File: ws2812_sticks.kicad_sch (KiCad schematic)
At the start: 11 parts, among them J1 Conn_01x03_Socket, J2 Conn_01x03_Socket

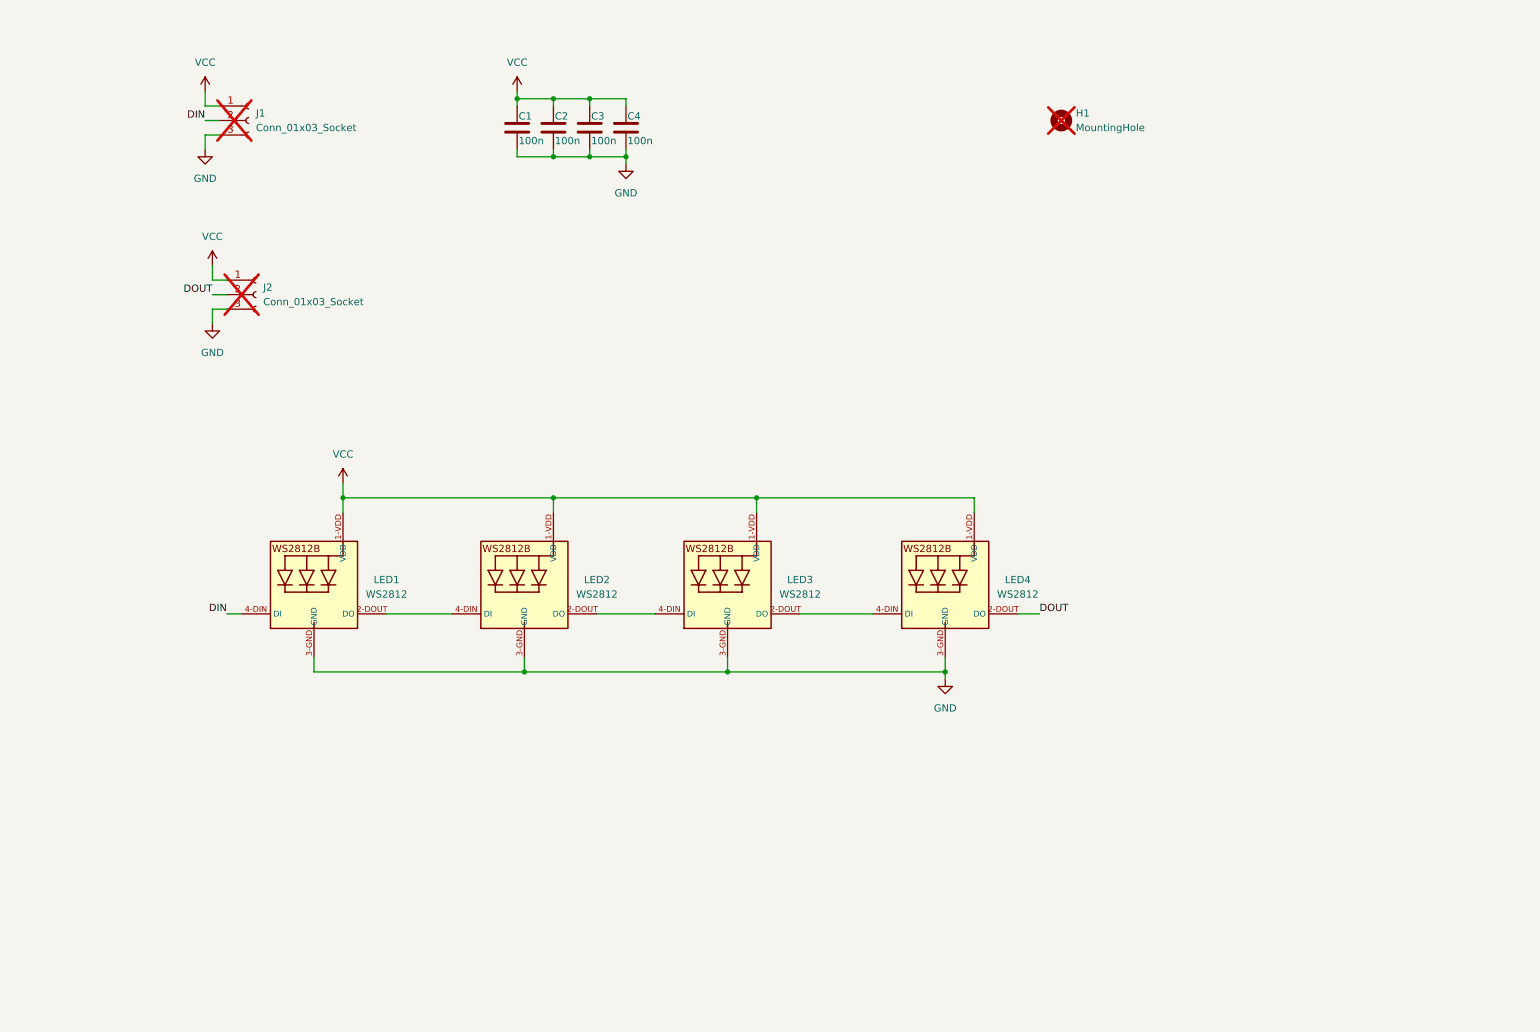
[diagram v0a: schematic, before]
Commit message: created 8 led version
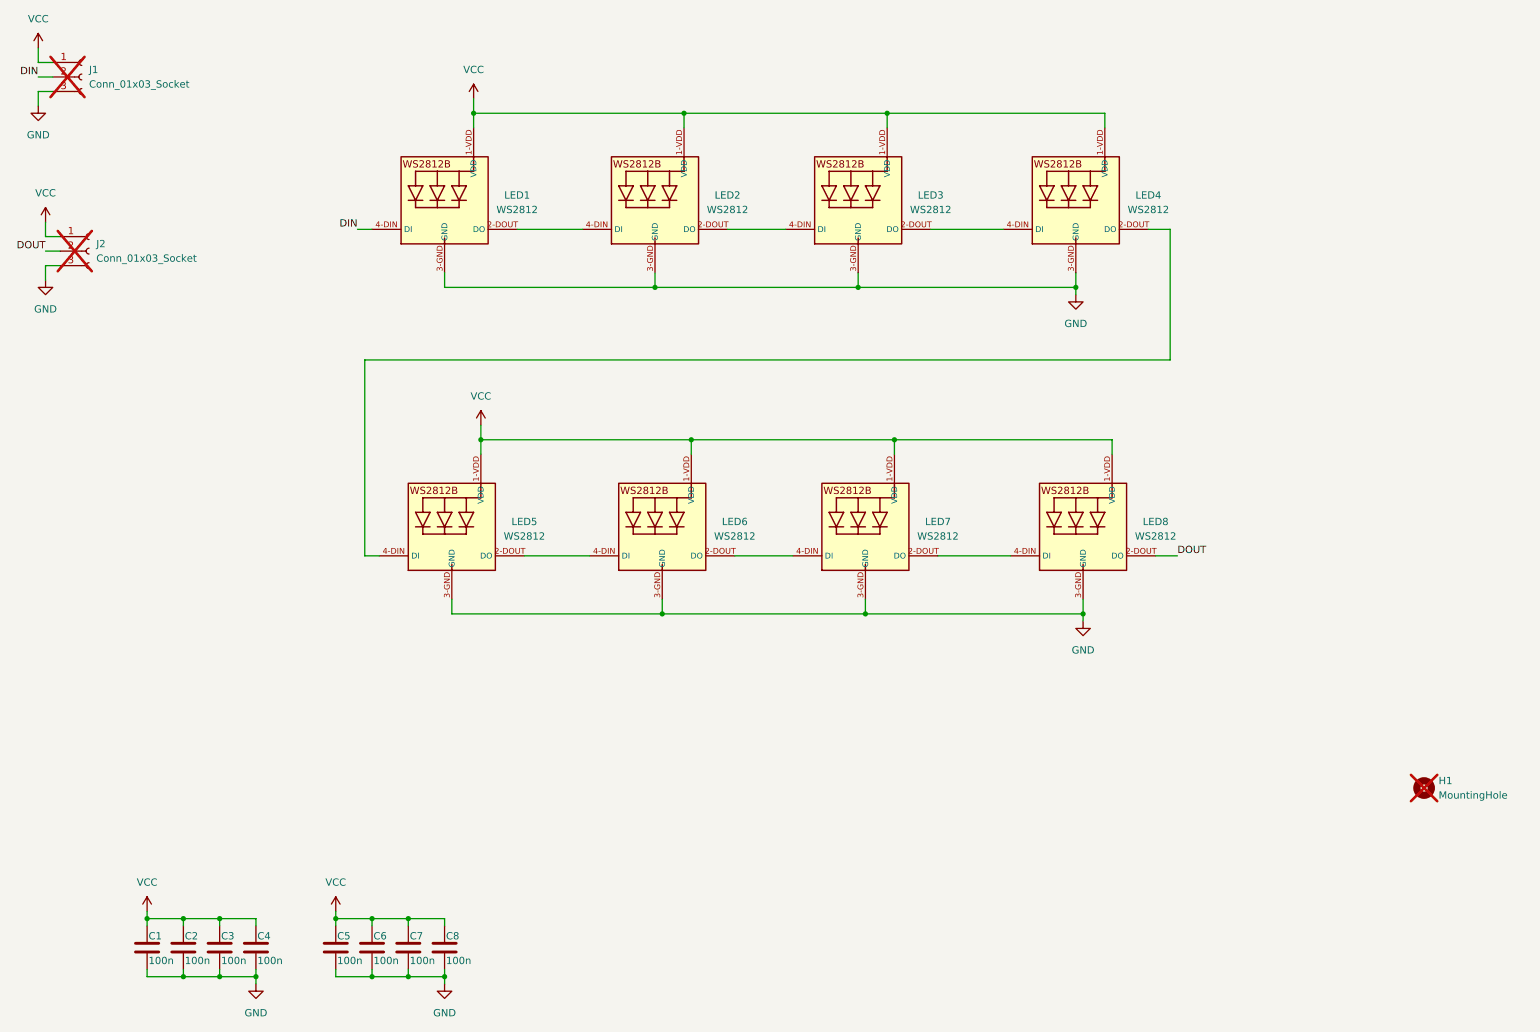
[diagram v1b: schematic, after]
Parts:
- added C5: 100n, 0Capacitors:C_0402_1005Metric, symbol 0Capacitors:0603_100n_50v
- added C6, C7, C8: 100n, 0Capacitors:C_0603_1608Metric, symbol 0Capacitors:0603_100n_50v
- added LED5, LED6, LED7, LED8: WS2812, 0LED:WS2812B_5050, symbol 0LEDs:WS2812_5050
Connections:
- net DOUT: now also LED8.2-DOUT (DO); no longer LED4.2-DOUT (DO)
- net GND: now also C5.2, C6.2, C7.2, C8.2, LED5.3-GND (GND), LED6.3-GND (GND), LED7.3-GND (GND), LED8.3-GND (GND)
- net VCC: now also C5.1, C6.1, C7.1, C8.1, LED5.1-VDD (VDD), LED6.1-VDD (VDD), LED7.1-VDD (VDD), LED8.1-VDD (VDD)
- new net: LED7.2-DOUT (DO), LED8.4-DIN (DI)
- new net: LED6.2-DOUT (DO), LED7.4-DIN (DI)
- new net: LED5.2-DOUT (DO), LED6.4-DIN (DI)
- new net: LED4.2-DOUT (DO), LED5.4-DIN (DI)
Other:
- moved on the sheet: C1, C2, C3, C4, H1, J1, J2, LED1, LED2, LED3, LED4
